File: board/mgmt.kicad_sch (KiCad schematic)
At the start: 36 parts, among them J2 CONN_01X05, J3 JUMPER_0402_SPDT, J4 JUMPER_0402_SPDT, J5 RJ45, SW1 SWITCH, SW2 SWITCH, SW3 SWITCH, SW4 SWITCH, U2 STM32F031-QFN28, U3 MAX232

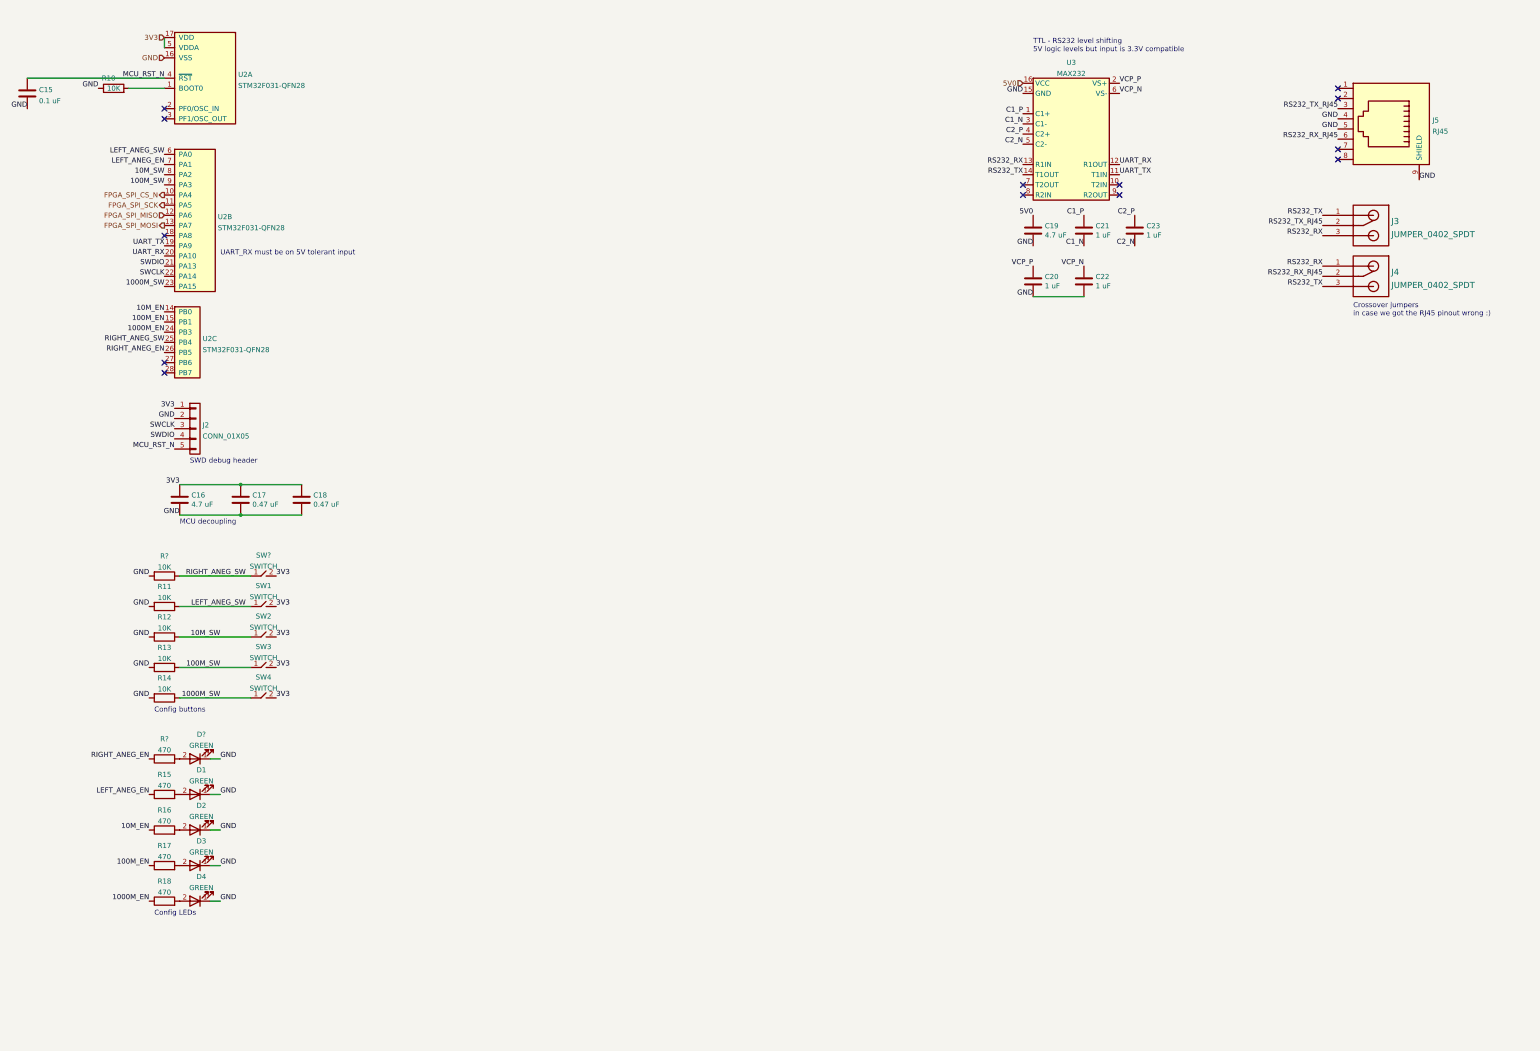
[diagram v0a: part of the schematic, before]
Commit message: Continued initial schematic capture
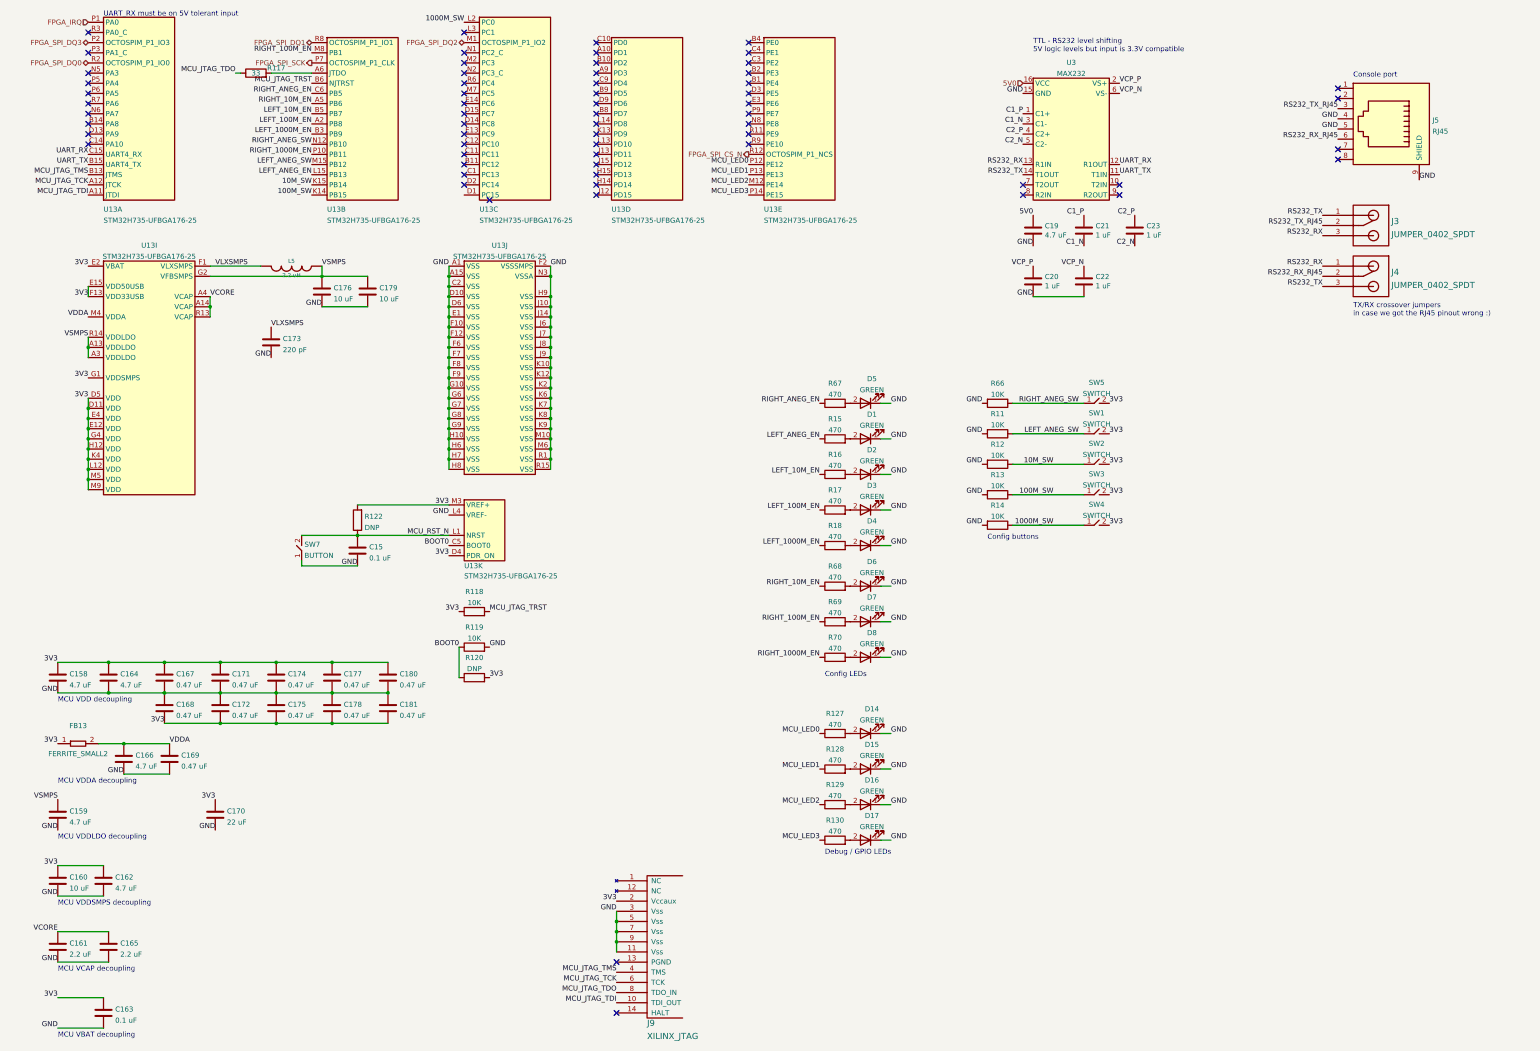
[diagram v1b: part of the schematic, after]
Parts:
- removed C16: 4.7 uF, azonenberg_pcb:EIA_0603_CAP_NOSILK, symbol device:C
- removed C17, C18: 0.47 uF, azonenberg_pcb:EIA_0402_CAP_NOSILK, symbol device:C
- removed J2: CONN_01X05, symbol conn:CONN_01X05
- removed R10: 10K, symbol device:R
- removed U2: STM32F031-QFN28, symbol st-azonenberg:STM32F031-QFN28
- added C158, C159, C162, C164, C166: 4.7 uF, azonenberg_pcb:EIA_0603_CAP_NOSILK, symbol device:C
- added C160, C176, C179: 10 uF, azonenberg_pcb:EIA_0805_CAP_NOSILK, symbol device:C
- added C161, C165: 2.2 uF, azonenberg_pcb:EIA_0603_CAP_NOSILK, symbol device:C
- added C163: 0.1 uF, azonenberg_pcb:EIA_0402_CAP_NOSILK, symbol device:C
- added C167, C168, C169, C171, C172, C174, C175, C177, C178, C180, C181: 0.47 uF, azonenberg_pcb:EIA_0402_CAP_NOSILK, symbol device:C
- added C170: 22 uF, azonenberg_pcb:EIA_1206_CAP_NOSILK, symbol device:C
- added C173: 220 pF, azonenberg_pcb:EIA_0402_CAP_NOSILK, symbol device:C
- added D14, D15, D16, D17, D6, D7, D8: GREEN, azonenberg_pcb:EIA_0603_LED, symbol device:LED
- added FB13: FERRITE_SMALL2, azonenberg_pcb:EIA_0603_INDUCTOR_NOSILK, symbol passive-azonenberg:FERRITE_SMALL2
- added J9: XILINX_JTAG, azonenberg_pcb:XILINX_JTAG_PTH_MOLEX_0878311420, symbol xilinx-azonenberg:XILINX_JTAG
- added L5: 2.2 uH, azonenberg_pcb:EIA_1210_CAP_NOSILK, symbol passive-azonenberg:INDUCTOR_PWROUT
- added R117: 33, azonenberg_pcb:EIA_0402_RES_NOSILK, symbol device:R
- added R118, R119: 10K, azonenberg_pcb:EIA_0402_RES_NOSILK, symbol device:R
- added R120, R122: DNP, azonenberg_pcb:EIA_0402_RES_NOSILK, symbol device:R
- added R127, R128, R129, R130, R68, R69, R70: 470, azonenberg_pcb:EIA_0402_RES_NOSILK, symbol device:R
- added SW7: BUTTON, symbol passive-azonenberg:SWITCH
- added U13: STM32H735-UFBGA176-25, azonenberg_pcb:BGA_201_10x10_DEPOP_0.65MM_OSHPARK, symbol st-azonenberg:STM32H735-UFBGA176-25
- D1, D2, D3, D4: footprint (none) -> azonenberg_pcb:EIA_0603_LED
- D5: renamed from D?; footprint (none) -> azonenberg_pcb:EIA_0603_LED
- J3, J4: footprint (none) -> azonenberg_pcb:EIA_0402_JUMPER
- J5: footprint (none) -> azonenberg_pcb:CONN_RJ45_BELSTEWART_SS-7188S-A-PG4-1-BA-xx
- R11, R12, R13, R14, R15, R16, R17, R18: footprint (none) -> azonenberg_pcb:EIA_0402_RES_NOSILK
- R66, R67: renamed from R?; footprint (none) -> azonenberg_pcb:EIA_0402_RES_NOSILK
- SW1, SW2, SW3, SW4: footprint (none) -> azonenberg_pcb:SWITCH_RAFI_MICON_5
- SW5: renamed from SW?; footprint (none) -> azonenberg_pcb:SWITCH_RAFI_MICON_5
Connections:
- net 1000M_SW: now also U13.L2 (PC0)
- net 100M_SW: now also U13.K14 (PB15)
- net 10M_SW: now also U13.K15 (PB14)
- net 3V3: now also C158.1, C160.1, C162.1, C163.1, C164.1, C167.1, C168.2, C170.1, C171.1, C172.2, C174.1, C175.2, C177.1, C178.2, C180.1, C181.2, FB13.1, J9.2 (Vccaux), R118.1, R120.2, R122.2, U13.D11 (VDD), U13.D4 (PDR_ON), U13.D5 (VDD), U13.E12 (VDD), U13.E15 (VDD50USB), U13.E2 (VBAT), U13.E4 (VDD), U13.F13 (VDD33USB), U13.G1 (VDDSMPS), U13.G4 (VDD), U13.H12 (VDD), U13.K4 (VDD), U13.L12 (VDD), U13.M3 (VREF+), U13.M5 (VDD), U13.M9 (VDD)
- net FPGA_SPI_CS_N: now also U13.R12 (PE11)
- net FPGA_SPI_SCK: now also U13.P7 (PB2)
- net GND: now also C158.2, C159.2, C160.2, C161.2, C162.2, C163.2, C164.2, C165.2, C166.2, C167.2, C168.1, C169.2, C170.2, C171.2, C172.1, C173.2, C174.2, C175.1, C176.2, C177.2, C178.1, C179.2, C180.2, C181.1, D14.1 (K), D15.1 (K), D16.1 (K), D17.1 (K), D6.1 (K), D7.1 (K), D8.1 (K), J9.11 (Vss), J9.3 (Vss), J9.5 (Vss), J9.7 (Vss), J9.9 (Vss), R119.2, SW7.1, U13.A1 (VSS), U13.A15 (VSS), U13.C2 (VSS), U13.D10 (VSS), U13.D6 (VSS), U13.E1 (VSS), U13.F10 (VSS), U13.F12 (VSS), U13.F2 (VSSSMPS), U13.F6 (VSS), U13.F7 (VSS), U13.F8 (VSS), U13.F9 (VSS), U13.G10 (VSS), U13.G6 (VSS), U13.G7 (VSS), U13.G8 (VSS), U13.G9 (VSS), U13.H10 (VSS), U13.H6 (VSS), U13.H7 (VSS), U13.H8 (VSS), U13.H9 (VSS), U13.J10 (VSS), U13.J14 (VSS), U13.J6 (VSS), U13.J7 (VSS), U13.J8 (VSS), U13.J9 (VSS), U13.K10 (VSS), U13.K12 (VSS), U13.K2 (VSS), U13.K6 (VSS), U13.K7 (VSS), U13.K8 (VSS), U13.K9 (VSS), U13.L4 (VREF-), U13.M10 (VSS), U13.M6 (VSS), U13.N3 (VSSA), U13.R1 (VSS), U13.R15 (VSS)
- net LEFT_ANEG_EN: now also U13.L15 (PB13)
- net LEFT_ANEG_SW: now also U13.M15 (PB12)
- net MCU_RST_N: now also R122.1, SW7.2, U13.L1 (NRST)
- net RIGHT_ANEG_EN: now also U13.C6 (PB5)
- net RIGHT_ANEG_SW: now also U13.N12 (PB10)
- net UART_RX: now also U13.C15 (PA11)
- net UART_TX: now also U13.B15 (PA12)
- net 1000M_EN renamed LEFT_1000M_EN
- net LEFT_1000M_EN: now also U13.B3 (PB9)
- net 100M_EN renamed LEFT_100M_EN
- net LEFT_100M_EN: now also U13.A2 (PB8)
- net 10M_EN renamed LEFT_10M_EN
- net LEFT_10M_EN: now also U13.B5 (PB7)
- new net: D6.2 (A), R68.2
- new net: R117.2, U13.A6 (PB3)
- new net: D14.2 (A), R127.2
- new net: D17.2 (A), R130.2
- new net: D7.2 (A), R69.2
- new net: D15.2 (A), R128.2
- new net: D8.2 (A), R70.2
- new net: D16.2 (A), R129.2
- new net BOOT0: R119.1, R120.1, U13.C5 (BOOT0)
- new net FPGA_IRQ: U13.P1 (PA0)
- new net FPGA_SPI_DQ0: U13.R2 (PA2)
- new net FPGA_SPI_DQ1: U13.R8 (PB0)
- new net FPGA_SPI_DQ2: U13.M1 (PC2)
- new net FPGA_SPI_DQ3: U13.P2 (PA1)
- new net MCU_JTAG_TCK: J9.6 (TCK), U13.A12 (PA14)
- new net MCU_JTAG_TDI: J9.10 (TDI_OUT), U13.A11 (PA15)
- new net MCU_JTAG_TDO: J9.8 (TDO_IN), R117.1
- new net MCU_JTAG_TMS: J9.4 (TMS), U13.B13 (PA13)
- new net MCU_JTAG_TRST: R118.2, U13.B6 (PB4)
- new net MCU_LED0: R127.1, U13.P12 (PE12)
- new net MCU_LED1: R128.1, U13.P13 (PE13)
- new net MCU_LED2: R129.1, U13.M12 (PE14)
- new net MCU_LED3: R130.1, U13.P14 (PE15)
- new net RIGHT_1000M_EN: R70.1, U13.P10 (PB11)
- new net RIGHT_100M_EN: R69.1, U13.M8 (PB1)
- new net RIGHT_10M_EN: R68.1, U13.A5 (PB6)
- new net VCORE: C161.1, C165.1, U13.A14 (VCAP), U13.A4 (VCAP), U13.R13 (VCAP)
- new net VDDA: C166.1, C169.1, FB13.2, U13.M4 (VDDA)
- new net VLXSMPS: C173.1, L5.2, U13.F1 (VLXSMPS)
- new net VSMPS: C159.1, C176.1, C179.1, L5.1, U13.A13 (VDDLDO), U13.A3 (VDDLDO), U13.G2 (VFBSMPS), U13.R14 (VDDLDO)
- no-connect marks 13 -> 63
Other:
- note added: "Console port"
- note added: "Debug / GPIO LEDs"
- note added: "MCU VBAT decoupling"
- note added: "MCU VCAP decoupling"
- note added: "MCU VDD decoupling"
- note added: "MCU VDDA decoupling"
- note added: "MCU VDDLDO decoupling"
- note added: "MCU VDDSMPS decoupling"
- note added: "TX/RX crossover jumpers in case we got the RJ45 pinout wrong :)"
- note removed: "Crossover jumpers in case we got the RJ45 pinout wrong :)"
- note removed: "MCU decoupling"
- note removed: "SWD debug header"
- moved on the sheet: C15, D1, D2, D3, D4, D5, R11, R12, R13, R14, R15, R16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

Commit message: Finished initial schematic, ready for signoff review
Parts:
- added TP10, TP9: U.FL, azonenberg_pcb:CONN_U.FL_TE_1909763-1, symbol conn:CONN_COAXIAL
- C15: footprint (none) -> azonenberg_pcb:EIA_0402_CAP_NOSILK
- C20, C21, C22, C23: footprint (none) -> azonenberg_pcb:EIA_0603_CAP_NOSILK
- SW7: footprint (none) -> azonenberg_pcb:SWITCH_RAFI_MICON_5
- U3: footprint (none) -> azonenberg_pcb:SOIC_16_3.9MM
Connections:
- net GND: now also TP10.2 (Ext), TP9.2 (Ext)
- net VCORE: now also TP10.1 (In)
- net VSMPS: now also TP9.1 (In)
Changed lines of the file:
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@@
   (no_connect (at 38.1 45.72))
   (no_connect (at 132.08 60.96))
-  (no_connect (at 138.43 64.77))
   (no_connect (at 203.2 25.4))
   (no_connect (at 203.2 27.94))
@@
   (no_connect (at 132.08 45.72))
   (no_connect (at 165.1 27.94))
+  (no_connect (at 132.08 63.5))
   (no_connect (at 165.1 63.5))
   (no_connect (at 165.1 60.96))
@@
     (stroke (width 0) (type default) (color 0 0 0 0))
   )
+  (wire (pts (xy 80.01 127) (xy 83.82 127))
+    (stroke (width 0) (type default) (color 0 0 0 0))
+  )
   (wire (pts (xy 71.12 195.58) (xy 85.09 195.58))
     (stroke (width 0) (type default) (color 0 0 0 0))
@@
   )
   (wire (pts (xy 153.67 96.52) (xy 153.67 99.06))
+    (stroke (width 0) (type default) (color 0 0 0 0))
+  )
+  (wire (pts (xy 80.01 116.84) (xy 83.82 116.84))
     (stroke (width 0) (type default) (color 0 0 0 0))
   )
@@
     (effects (font (size 1.27 1.27)) (justify right bottom))
   )
-  (label "GND" (at 128.27 81.28 180)
-    (effects (font (size 1.27 1.27)) (justify right bottom))
-  )
   (label "VCP_P" (at 295.91 35.56 0)
     (effects (font (size 1.27 1.27)) (justify left bottom))
@@
     (effects (font (size 1.27 1.27)) (justify left bottom))
   )
+  (label "VCORE" (at 80.01 121.92 180)
+    (effects (font (size 1.27 1.27)) (justify right bottom))
+  )
   (label "GND" (at 350.52 44.45 180)
     (effects (font (size 1.27 1.27)) (justify right bottom))
@@
     (effects (font (size 1.27 1.27)) (justify right bottom))
   )
+  (label "VSMPS" (at 80.01 111.76 180)
+    (effects (font (size 1.27 1.27)) (justify right bottom))
+  )
   (label "RIGHT_ANEG_EN" (at 220.98 115.57 180)
     (effects (font (size 1.27 1.27)) (justify right bottom))
@@
     (effects (font (size 1.27 1.27)) (justify left bottom))
   )
-  (label "3V3" (at 38.1 81.28 180)
-    (effects (font (size 1.27 1.27)) (justify right bottom))
-  )
   (label "3V3" (at 30.48 180.34 180)
     (effects (font (size 1.27 1.27)) (justify right bottom))
@@
     (effects (font (size 1.27 1.27)) (justify right bottom))
   )
+  (label "GND" (at 80.01 127 180)
+    (effects (font (size 1.27 1.27)) (justify right bottom))
+  )
   (label "3V3" (at 170.18 240.03 180)
     (effects (font (size 1.27 1.27)) (justify right bottom))
@@
   )
   (label "RIGHT_ANEG_SW" (at 285.75 115.57 180)
+    (effects (font (size 1.27 1.27)) (justify right bottom))
+  )
+  (label "GND" (at 80.01 116.84 180)
     (effects (font (size 1.27 1.27)) (justify right bottom))
   )
@@
     (effects (font (size 1.27 1.27)) (justify right))
   )
+  (hierarchical_label "3V3" (shape input) (at 38.1 81.28 180)
+    (effects (font (size 1.27 1.27)) (justify right))
+  )
   (hierarchical_label "FPGA_SPI_DQ0" (shape bidirectional) (at 38.1 30.48 180)
     (effects (font (size 1.27 1.27)) (justify right))
   )
   (hierarchical_label "FPGA_SPI_DQ1" (shape bidirectional) (at 93.98 25.4 180)
+    (effects (font (size 1.27 1.27)) (justify right))
+  )
+  (hierarchical_label "GND" (shape input) (at 128.27 81.28 180)
     (effects (font (size 1.27 1.27)) (justify right))
   )
@@
       (effects (font (size 1.27 1.27)) (justify right))
     )
-    (property "Footprint" "" (id 2) (at 91.44 152.4 0)
+    (property "Footprint" "azonenberg_pcb:SWITCH_RAFI_MICON_5" (id 2) (at 91.44 152.4 0)
       (effects (font (size 1.27 1.27)) hide)
     )
@@
       (effects (font (size 1.27 1.27)) (justify left))
     )
-    (property "Footprint" "" (id 2) (at 287.9852 88.9 0)
+    (property "Footprint" "azonenberg_pcb:EIA_0603_CAP_NOSILK" (id 2) (at 287.9852 88.9 0)
       (effects (font (size 1.27 1.27)) hide)
     )
@@
       (effects (font (size 1.27 1.27)) (justify left))
     )
-    (property "Footprint" "" (id 2) (at 106.3752 156.21 0)
+    (property "Footprint" "azonenberg_pcb:EIA_0402_CAP_NOSILK" (id 2) (at 106.3752 156.21 0)
       (effects (font (size 1.27 1.27)) hide)
     )
@@
       (effects (font (size 1.27 1.27)) (justify left))
     )
-    (property "Footprint" "" (id 2) (at 275.2852 88.9 0)
+    (property "Footprint" "azonenberg_pcb:EIA_0603_CAP_NOSILK" (id 2) (at 275.2852 88.9 0)
       (effects (font (size 1.27 1.27)) hide)
     )
@@
       (effects (font (size 1.27 1.27)) (justify left))
     )
-    (property "Footprint" "" (id 2) (at 300.6852 76.2 0)
+    (property "Footprint" "azonenberg_pcb:EIA_0603_CAP_NOSILK" (id 2) (at 300.6852 76.2 0)
       (effects (font (size 1.27 1.27)) hide)
     )
@@
     )
     (property "Datasheet" "" (id 3) (at 30.48 234.95 0)
+      (effects (font (size 1.27 1.27)) hide)
+    )
+    (pin "1")
+    (pin "2")
+  )
+  (symbol (lib_id "conn:CONN_COAXIAL") (at 83.82 111.76 0) (unit 1)
+    (in_bom yes) (on_board yes) (fields_autoplaced)
+    (property "Reference" "TP9" (id 0) (at 86.3601 111.1447 0)
+      (effects (font (size 1.27 1.27)) (justify left))
+    )
+    (property "Value" "U.FL" (id 1) (at 86.3601 113.9198 0)
+      (effects (font (size 1.27 1.27)) (justify left))
+    )
+    (property "Footprint" "azonenberg_pcb:CONN_U.FL_TE_1909763-1" (id 2) (at 83.82 111.76 0)
+      (effects (font (size 1.27 1.27)) hide)
+    )
+    (property "Datasheet" "" (id 3) (at 83.82 111.76 0)
       (effects (font (size 1.27 1.27)) hide)
     )
@@
     (property "Reference" "U3" (id 0) (at 283.845 30.3743 0))
     (property "Value" "MAX232" (id 1) (at 283.845 33.1494 0))
-    (property "Footprint" "" (id 2) (at 274.32 40.64 0)
+    (property "Footprint" "azonenberg_pcb:SOIC_16_3.9MM" (id 2) (at 274.32 40.64 0)
       (effects (font (size 1.27 1.27)) hide)
     )
@@
     )
     (property "Datasheet" "" (id 3) (at 99.06 184.15 0)
+      (effects (font (size 1.27 1.27)) hide)
+    )
+    (pin "1")
+    (pin "2")
+  )
+  (symbol (lib_id "conn:CONN_COAXIAL") (at 83.82 121.92 0) (unit 1)
+    (in_bom yes) (on_board yes) (fields_autoplaced)
+    (property "Reference" "TP10" (id 0) (at 86.3601 121.3047 0)
+      (effects (font (size 1.27 1.27)) (justify left))
+    )
+    (property "Value" "U.FL" (id 1) (at 86.3601 124.0798 0)
+      (effects (font (size 1.27 1.27)) (justify left))
+    )
+    (property "Footprint" "azonenberg_pcb:CONN_U.FL_TE_1909763-1" (id 2) (at 83.82 121.92 0)
+      (effects (font (size 1.27 1.27)) hide)
+    )
+    (property "Datasheet" "" (id 3) (at 83.82 121.92 0)
       (effects (font (size 1.27 1.27)) hide)
     )
@@
       (effects (font (size 1.27 1.27)) (justify left))
     )
-    (property "Footprint" "" (id 2) (at 287.9852 76.2 0)
-      (effects (font (size 1.27 1.27)) hide)
-    )
+    (property "Footprint" "azonenberg_pcb:EIA_0603_CAP_NOSILK" (id 2) (at 287.9852 76.2 0)
+      (effects (font (size 1.27 1.27)) hide)
+    )
